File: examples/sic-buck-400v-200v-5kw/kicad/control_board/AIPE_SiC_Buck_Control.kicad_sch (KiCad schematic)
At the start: 0 parts

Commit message: feat(v2.1): example regenerated - wired schematics, both boards routed with the upgraded router, exports, crops, validation
Schematics (wired style, gates passed): ERC 0 on both projects (power 20261012T075113Z-erc-df18ce6e,
control 20261012T075120Z-erc-7a14cacb); netlist (ref,pad)->net exact vs the model and vs the frozen V2
netlists with equal net names; .kicad_dru / net_settings identical to the legacy generation; stub
global labels 648 -> 7 (power) and 667 -> 7 (control), wired pin share 0 -> 0.90 / 0.76, junctions,
hierarchical labels and power symbols introduced, continuation sheets removed; readability metrics
V2 vs V2.1 in engineering_checks/schematic_readability_*.

Power board (octilinear simplification + tangent arcs on the V2 search; 8-direction search kept
opt-in after attempt A left 2 connections open): 0 unresolved, DRC 0/0/0 (20261012T090308Z-drc-8fd50803),
segments 4755 -> 2991 + 145 arcs, 90-degree bends 3609 -> 1121, stair runs 382 -> 124, length
5744.6 -> 5545.6 mm, vias 606 = V2, no net longer / more vias / narrower. Control board: 0 unresolved,
DRC 0/0/0 (20261012T084327Z-drc-7f07f983), segments 5995 -> 4262 + 261 arcs, 90-degree bends
4069 -> 1233, stair runs 435 -> 144, length 7055.2 -> 6700.7 mm, vias 798 = V2, 96 nets shorter,
0 longer. FOOTPRINT.SetDNP for DNP parts (schematic parity), beautify anchors bound to off-grid vias
by copper overlap (path_geometry.connected_by_overlap), In2.Cu inner pass styled.

Exports 11/11 per board, renders and layer PDFs refreshed, high-resolution V2/V2.1 crops under
review/crops/, routing_quality_* and v21_validation.{json,md} (nine TASK 7 checks independently
re-derived). verify_sic_buck passed; 338 tests OK (2 skipped).

Co-Authored-By: Claude Fable 5.1 <noreply@anthropic.com>
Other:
- removed sheet PWM gating, fault latch, combiners, comparators (2)
- sheet 12 V entry, TVS and TPS26400 eFuse ports: added FLT_12V_N, I12V_MON, V12V_MON; removed none
- sheet 5 V buck, dual LDO, supervisor and reset ports: added XRS_N; removed none
- sheet ADC conditioning, NTC readout, monitors ports: added ADC_I12V, ADC_ISENSE, ADC_ISENSE_REF, ADC_TEMP_CTRL, ADC_TEMP_HS, ADC_V12V, ADC_VIN, ADC_VOUT, I12V_MON, ISENSE, ISENSE_REF, OTP_REF, TEMP_HS_NTC, V12V_MON, VIN_SENSE, VOUT_SENSE; removed none
- sheet DSP per-pin bypass and ADC reference ports: added ADCREFM, ADCREFP, ADCRESEXT; removed none
- sheet Mezzanine header, connectors, LEDs, test points, mounting ports: added ARM, BIAS_EN, FAN_TACH, FAULT_LATCH_N, FAULT_N, FLT_H_N, FLT_L_N, GATE_EN, ISENSE, ISENSE_REF, LED_FAULT, LED_RUN, OC_N, PG_BIAS_H_N, PG_BIAS_L_N, PG_BIAS_S_N, PWM_H, PWM_L, RDY_H, RDY_L, RELAY_ON, RESET_N, SPARE_D1, SPARE_D2, VIN_SENSE, VOUT_SENSE, XRS_N; removed none
- sheet Oscillator, boot straps, JTAG, UART ports: added BOOT84, BOOT85, BOOT86, BOOT87, CLK30, EMU0, EMU1, TCK, TDI, TDO, TMS, TRST, UART_RX, UART_TX; removed none
- sheet PWM gating, fault latch, combiners, comparators ports: added ARM, DSP_TRIP_N, EPWM1A, EPWM1B, ESTOP_N, FAULT_LATCH_N, FAULT_N, FLT_12V_N, FLT_H_N, FLT_L_N, GATE_EN, OC_N, OTP_N, OTP_REF, OVP_N, PG_BIAS_H_N, PG_BIAS_L_N, PG_BIAS_S_N, PWM_H, PWM_L, RDY_H, RDY_L, TEMP_HS_NTC, UVLO_N, VIN_SENSE, VOUT_SENSE, XRS_N; removed none
- sheet TMS320F28335 - all 176 pins ports: added ADCREFM, ADCREFP, ADCRESEXT, ADC_I12V, ADC_ISENSE, ADC_ISENSE_REF, ADC_TEMP_CTRL, ADC_TEMP_HS, ADC_V12V, ADC_VIN, ADC_VOUT, ARM, BIAS_EN, BOOT84, BOOT85, BOOT86, BOOT87, CLK30, DSP_TRIP_N, EMU0, EMU1, EPWM1A, EPWM1B, ESTOP_N, FAN_TACH, FAULT_N, FLT_12V_N, FLT_H_N, FLT_L_N, LED_FAULT, LED_RUN, OC_N, OTP_N, OVP_N, PG_BIAS_H_N, PG_BIAS_L_N, PG_BIAS_S_N, RDY_H, RDY_L, RELAY_ON, RESET_N, SPARE_D1, SPARE_D2, TCK, TDI, TDO, TMS, TRST, UART_RX, UART_TX, UVLO_N, XRS_N; removed none

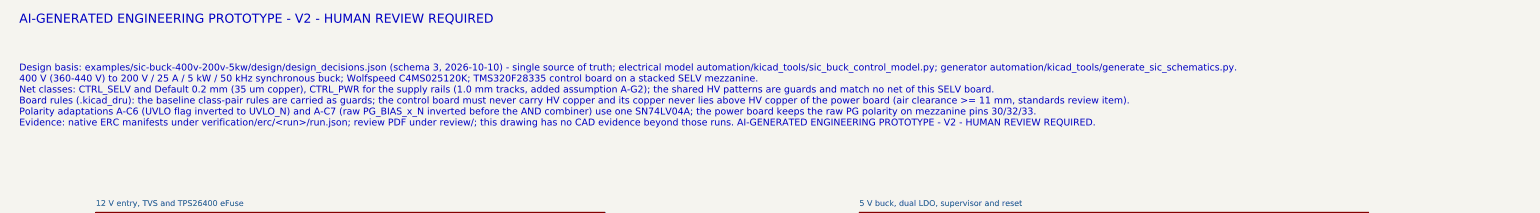
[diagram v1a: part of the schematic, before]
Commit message: chore(v2.1): one generation label (sic_buck_common.GENERATION) and a reproducible full regeneration
GENERATION = "V2.1" derives BANNER, REVISION, title-block comments, .kicad_dru headers,
NOTICE.md, the power-board silkscreen and the control-board label (kept at the V2 label
length so the placer's text obstacle box, and therefore the placement, is unchanged).
Models, schematics (ERC 0: 20261012T094955Z-erc-c574a866 / 20261012T095007Z-erc-caa10a79,
all gates passed), both boards (DRC 0/0/0: power 20261012T100423Z-drc-8b9e64d1, control
20261012T103755Z-drc-0a4fa5cf), netlist checks, routing-quality records (totals, per-layer
and per-net tables identical to the previous commit), exports (11/11 each), renders, V2.1
crops (same framing; V2 crops untouched) and readability reports regenerated. Independent
re-validation in verification/v21_validation.{json,md} (12 rows). verify_sic_buck passed;
340 tests OK (2 skipped). Known residue: control-board corridor zone priorities depend on
reload order (same zones, DRC clean), manufacturing/README.md still describes the V2 bundle.

Co-Authored-By: Claude Fable 5.1 <noreply@anthropic.com>
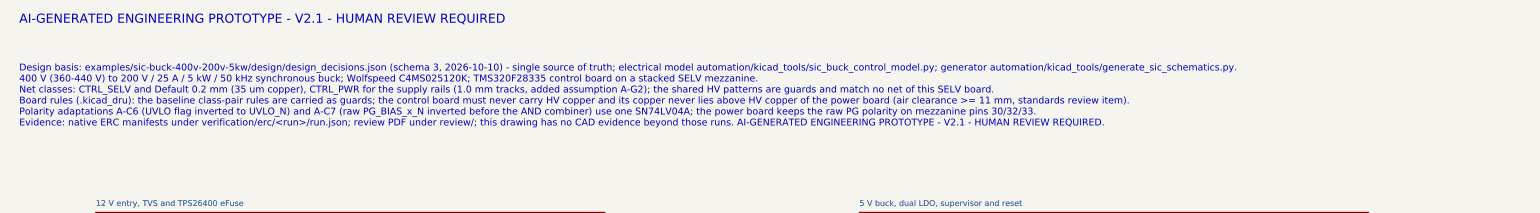
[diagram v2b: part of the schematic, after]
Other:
- note added: "AI-GENERATED ENGINEERING PROTOTYPE - V2.1 - HUMAN REVIEW REQUIRED"
- note removed: "AI-GENERATED ENGINEERING PROTOTYPE - V2 - HUMAN REVIEW REQUIRED"
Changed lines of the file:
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@@
  (paper "A2")
           (title_block (title "AIPE V2 SiC buck control board - 400 V (360-440 V) to 200 V / 25 A / 5 kW / 50 kHz synchronous buck; Wolfspeed C4MS025120K; TMS320F28335 control board on a stacked SELV mezzanine") (rev "V2.1")
-            (comment 1 "AI-GENERATED ENGINEERING PROTOTYPE - V2 - HUMAN REVIEW REQUIRED"))
-          (text "AI-GENERATED ENGINEERING PROTOTYPE - V2 - HUMAN REVIEW REQUIRED" (at 20 20 0)
+            (comment 1 "AI-GENERATED ENGINEERING PROTOTYPE - V2.1 - HUMAN REVIEW REQUIRED"))
+          (text "AI-GENERATED ENGINEERING PROTOTYPE - V2.1 - HUMAN REVIEW REQUIRED" (at 20 20 0)
           (effects (font (size 2 2)) (justify left top))
 )
-(text "Design basis: examples/sic-buck-400v-200v-5kw/design/design_decisions.json (schema 3, 2026-10-10) - single source of truth; electrical model automation/kicad_tools/sic_buck_control_model.py; generator automation/kicad_tools/generate_sic_schematics.py.\n400 V (360-440 V) to 200 V / 25 A / 5 kW / 50 kHz synchronous buck; Wolfspeed C4MS025120K; TMS320F28335 control board on a stacked SELV mezzanine.\nNet classes: CTRL_SELV and Default 0.2 mm (35 um copper), CTRL_PWR for the supply rails (1.0 mm tracks, added assumption A-G2); the shared HV patterns are guards and match no net of this SELV board.\nBoard rules (.kicad_dru): the baseline class-pair rules are carried as guards; the control board must never carry HV copper and its copper never lies above HV copper of the power board (air clearance >= 11 mm, standards review item).\nPolarity adaptations A-C6 (UVLO flag inverted to UVLO_N) and A-C7 (raw PG_BIAS_x_N inverted before the AND combiner) use one SN74LV04A; the power board keeps the raw PG polarity on mezzanine pins 30/32/33.\nEvidence: native ERC manifests under verification/erc/<run>/run.json; review PDF under review/; this drawing has no CAD evidence beyond those runs. AI-GENERATED ENGINEERING PROTOTYPE - V2 - HUMAN REVIEW REQUIRED." (at 20 31 0)
+(text "Design basis: examples/sic-buck-400v-200v-5kw/design/design_decisions.json (schema 3, 2026-10-10) - single source of truth; electrical model automation/kicad_tools/sic_buck_control_model.py; generator automation/kicad_tools/generate_sic_schematics.py.\n400 V (360-440 V) to 200 V / 25 A / 5 kW / 50 kHz synchronous buck; Wolfspeed C4MS025120K; TMS320F28335 control board on a stacked SELV mezzanine.\nNet classes: CTRL_SELV and Default 0.2 mm (35 um copper), CTRL_PWR for the supply rails (1.0 mm tracks, added assumption A-G2); the shared HV patterns are guards and match no net of this SELV board.\nBoard rules (.kicad_dru): the baseline class-pair rules are carried as guards; the control board must never carry HV copper and its copper never lies above HV copper of the power board (air clearance >= 11 mm, standards review item).\nPolarity adaptations A-C6 (UVLO flag inverted to UVLO_N) and A-C7 (raw PG_BIAS_x_N inverted before the AND combiner) use one SN74LV04A; the power board keeps the raw PG polarity on mezzanine pins 30/32/33.\nEvidence: native ERC manifests under verification/erc/<run>/run.json; review PDF under review/; this drawing has no CAD evidence beyond those runs. AI-GENERATED ENGINEERING PROTOTYPE - V2.1 - HUMAN REVIEW REQUIRED." (at 20 31 0)
           (effects (font (size 1.5 1.5)) (justify left top))
 )
